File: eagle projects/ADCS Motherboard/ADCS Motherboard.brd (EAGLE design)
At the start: 91 x 91 mm, 120 parts, among them J1 HDR_10_EZFET_DEBUGGER, J3 HDR_2X5_GRPB052VWQS-RC, Q1 PMV16XN, Q2 IRLML6246TRPBF, Q3 IRLML2246TRPBF, U1 MSP430F5529IPN, U2 LMV321, U3 ADS7841E_2K5, U4 LMV321, U5 LMV321, U7 HMC1053, Y1 32.768kHz, Y2 CSTCR4M00G15L99, Y3 32.768kHz

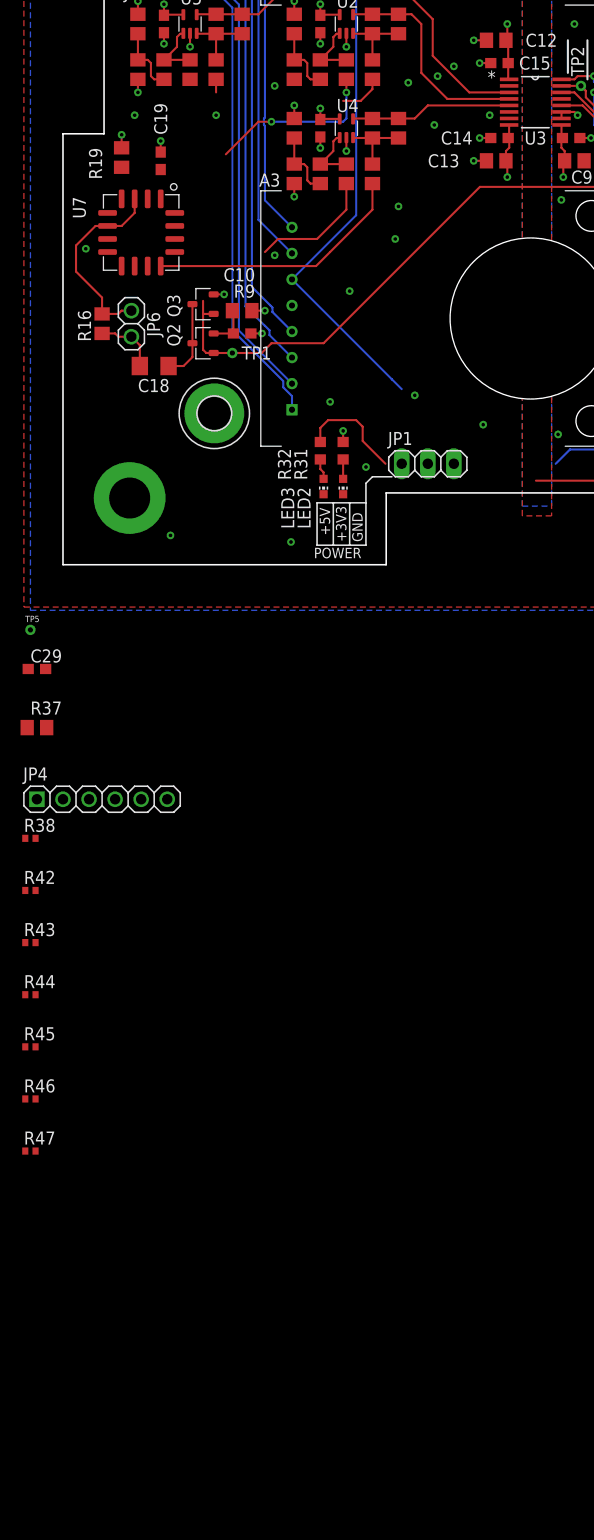
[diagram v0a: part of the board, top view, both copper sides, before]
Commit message: Added 5.1M ohms to BNO055 no connect pins
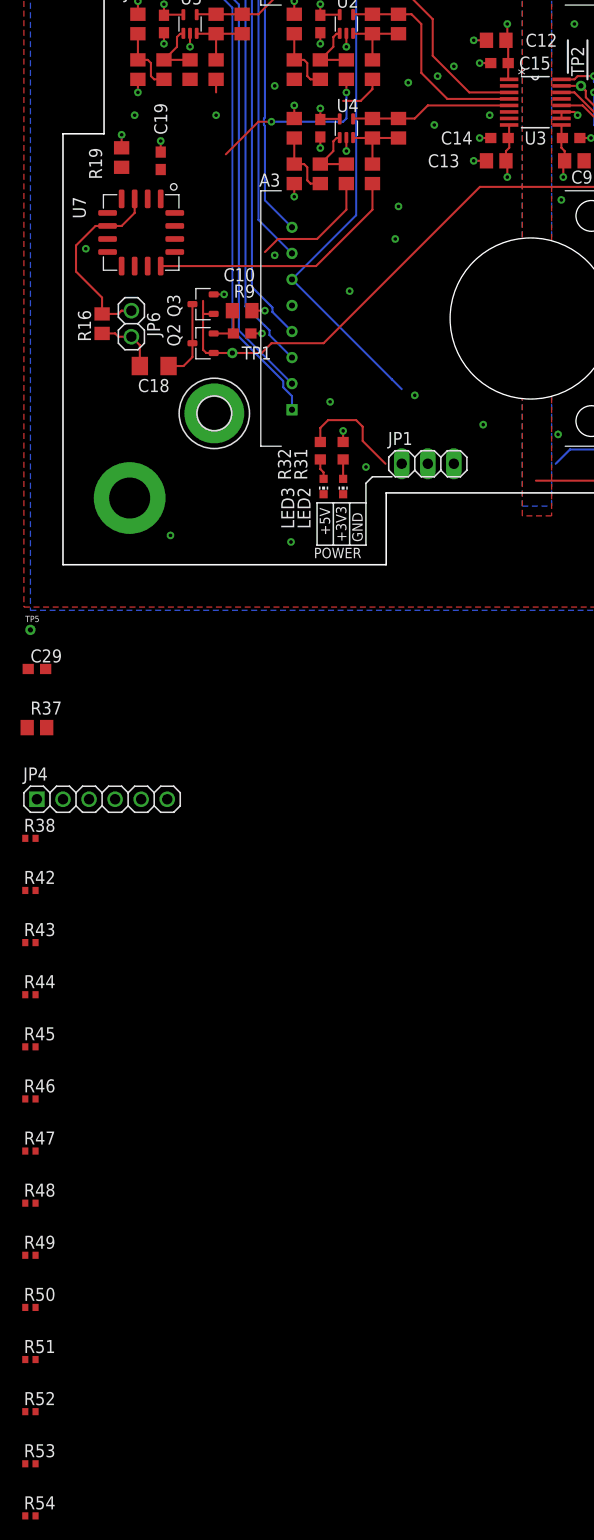
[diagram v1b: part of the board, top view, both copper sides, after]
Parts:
- added R48, R49, R50, R51, R52, R53, R54: 5.1M, rcl:R0402
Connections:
- new net N$40: R48.2, U6.1
- new net N$42: R49.2, U6.12
- new net N$43: R50.2, U6.13
- new net N$44: R51.2, U6.21
- new net N$45: R52.2, U6.22
- new net N$46: R53.2, U6.23
- new net N$47: R54.2, U6.24
- net GND: now also R48.1, R49.1, R50.1, R51.1, R52.1, R53.1, R54.1
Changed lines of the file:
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@@
 <attribute name="NAME" x="87.9475" y="13.97" size="1.27" layer="25" ratio="10" rot="R270"/>
 </element>
-<element name="U3" library="my_library" library_urn="urn:adsk.eagle:library:22876504" package="DBQ16" package3d_urn="urn:adsk.eagle:package:23087509/5" value="ADS7841E_2K5" x="46.0375" y="45.085" smashed="yes">
+<element name="U3" library="my_library" library_urn="urn:adsk.eagle:library:22876504" package="DBQ16" package3d_urn="urn:adsk.eagle:package:23087509/6" value="ADS7841E_2K5" x="46.0375" y="45.085" smashed="yes">
 <attribute name="DATASHEET_URL" value="http://www.ti.com/lit/gpn/ADS7841" x="71.4375" y="9.525" size="1.778" layer="27" display="off"/>
 <attribute name="DESCRIPTION" value="12-Bit, 4-Channel Serial Output Sampling Analog-to-Digital Converter" x="71.4375" y="9.525" size="1.778" layer="27" display="off"/>
@@
 <attribute name="SPICEPREFIX" value="R" x="-3.175" y="-57.15" size="1.778" layer="27" display="off"/>
 <attribute name="VALUE" x="-3.81" y="-59.055" size="1.27" layer="27"/>
+</element>
+<element name="R48" library="rcl" library_urn="urn:adsk.eagle:library:334" package="R0402" package3d_urn="urn:adsk.eagle:package:23547/3" value="5.1M" x="-3.175" y="-62.23" smashed="yes">
+<attribute name="NAME" x="-3.81" y="-61.595" size="1.27" layer="25"/>
+<attribute name="POPULARITY" value="34" x="-3.175" y="-62.23" size="1.778" layer="27" display="off"/>
+<attribute name="SPICEPREFIX" value="R" x="-3.175" y="-62.23" size="1.778" layer="27" display="off"/>
+<attribute name="VALUE" x="-3.81" y="-64.135" size="1.27" layer="27"/>
+</element>
+<element name="R49" library="rcl" library_urn="urn:adsk.eagle:library:334" package="R0402" package3d_urn="urn:adsk.eagle:package:23547/3" value="5.1M" x="-3.175" y="-67.31" smashed="yes">
+<attribute name="NAME" x="-3.81" y="-66.675" size="1.27" layer="25"/>
+<attribute name="POPULARITY" value="34" x="-3.175" y="-67.31" size="1.778" layer="27" display="off"/>
+<attribute name="SPICEPREFIX" value="R" x="-3.175" y="-67.31" size="1.778" layer="27" display="off"/>
+<attribute name="VALUE" x="-3.81" y="-69.215" size="1.27" layer="27"/>
+</element>
+<element name="R50" library="rcl" library_urn="urn:adsk.eagle:library:334" package="R0402" package3d_urn="urn:adsk.eagle:package:23547/3" value="5.1M" x="-3.175" y="-72.39" smashed="yes">
+<attribute name="NAME" x="-3.81" y="-71.755" size="1.27" layer="25"/>
+<attribute name="POPULARITY" value="34" x="-3.175" y="-72.39" size="1.778" layer="27" display="off"/>
+<attribute name="SPICEPREFIX" value="R" x="-3.175" y="-72.39" size="1.778" layer="27" display="off"/>
+<attribute name="VALUE" x="-3.81" y="-74.295" size="1.27" layer="27"/>
+</element>
+<element name="R51" library="rcl" library_urn="urn:adsk.eagle:library:334" package="R0402" package3d_urn="urn:adsk.eagle:package:23547/3" value="5.1M" x="-3.175" y="-77.47" smashed="yes">
+<attribute name="NAME" x="-3.81" y="-76.835" size="1.27" layer="25"/>
+<attribute name="POPULARITY" value="34" x="-3.175" y="-77.47" size="1.778" layer="27" display="off"/>
+<attribute name="SPICEPREFIX" value="R" x="-3.175" y="-77.47" size="1.778" layer="27" display="off"/>
+<attribute name="VALUE" x="-3.81" y="-79.375" size="1.27" layer="27"/>
+</element>
+<element name="R52" library="rcl" library_urn="urn:adsk.eagle:library:334" package="R0402" package3d_urn="urn:adsk.eagle:package:23547/3" value="5.1M" x="-3.175" y="-82.55" smashed="yes">
+<attribute name="NAME" x="-3.81" y="-81.915" size="1.27" layer="25"/>
+<attribute name="POPULARITY" value="34" x="-3.175" y="-82.55" size="1.778" layer="27" display="off"/>
+<attribute name="SPICEPREFIX" value="R" x="-3.175" y="-82.55" size="1.778" layer="27" display="off"/>
+<attribute name="VALUE" x="-3.81" y="-84.455" size="1.27" layer="27"/>
+</element>
+<element name="R53" library="rcl" library_urn="urn:adsk.eagle:library:334" package="R0402" package3d_urn="urn:adsk.eagle:package:23547/3" value="5.1M" x="-3.175" y="-87.63" smashed="yes">
+<attribute name="NAME" x="-3.81" y="-86.995" size="1.27" layer="25"/>
+<attribute name="POPULARITY" value="34" x="-3.175" y="-87.63" size="1.778" layer="27" display="off"/>
+<attribute name="SPICEPREFIX" value="R" x="-3.175" y="-87.63" size="1.778" layer="27" display="off"/>
+<attribute name="VALUE" x="-3.81" y="-89.535" size="1.27" layer="27"/>
+</element>
+<element name="R54" library="rcl" library_urn="urn:adsk.eagle:library:334" package="R0402" package3d_urn="urn:adsk.eagle:package:23547/3" value="5.1M" x="-3.175" y="-92.71" smashed="yes">
+<attribute name="NAME" x="-3.81" y="-92.075" size="1.27" layer="25"/>
+<attribute name="POPULARITY" value="34" x="-3.175" y="-92.71" size="1.778" layer="27" display="off"/>
+<attribute name="SPICEPREFIX" value="R" x="-3.175" y="-92.71" size="1.778" layer="27" display="off"/>
+<attribute name="VALUE" x="-3.81" y="-94.615" size="1.27" layer="27"/>
 </element>
 </elements>
@@
 <contactref element="R47" pad="2"/>
 <contactref element="U7" pad="15"/>
+<contactref element="R48" pad="1"/>
+<contactref element="R54" pad="1"/>
+<contactref element="R49" pad="1"/>
+<contactref element="R50" pad="1"/>
+<contactref element="R51" pad="1"/>
+<contactref element="R52" pad="1"/>
+<contactref element="R53" pad="1"/>
 <wire x1="73.025" y1="87.1056" x2="78.4225" y2="86.995" width="0" layer="19" extent="1-1"/>
 <wire x1="68.8975" y1="86.995" x2="73.025" y2="87.1056" width="0" layer="19" extent="1-1"/>
@@
 <wire x1="-2.675" y1="-52.07" x2="-2.675" y2="-46.99" width="0" layer="19" extent="1-1"/>
 <wire x1="-2.675" y1="-57.15" x2="-2.675" y2="-52.07" width="0" layer="19" extent="1-1"/>
+<wire x1="-3.675" y1="-62.23" x2="-2.675" y2="-57.15" width="0" layer="19" extent="1-1"/>
+<wire x1="-3.675" y1="-67.31" x2="-3.675" y2="-62.23" width="0" layer="19" extent="1-1"/>
+<wire x1="-3.675" y1="-72.39" x2="-3.675" y2="-67.31" width="0" layer="19" extent="1-1"/>
+<wire x1="-3.675" y1="-77.47" x2="-3.675" y2="-72.39" width="0" layer="19" extent="1-1"/>
+<wire x1="-3.675" y1="-82.55" x2="-3.675" y2="-77.47" width="0" layer="19" extent="1-1"/>
+<wire x1="-3.675" y1="-87.63" x2="-3.675" y2="-82.55" width="0" layer="19" extent="1-1"/>
+<wire x1="-3.675" y1="-92.71" x2="-3.675" y2="-87.63" width="0" layer="19" extent="1-1"/>
 <wire x1="10.16" y1="-22.86" x2="-3.675" y2="-26.67" width="0" layer="19" extent="1-1"/>
 </signal>
@@
 <wire x1="-3.675" y1="-57.15" x2="74.575" y2="42.2" width="0" layer="19" extent="1-1"/>
 </signal>
+<signal name="N$40">
+<contactref element="R48" pad="2"/>
+<contactref element="U6" pad="1"/>
+<wire x1="-2.675" y1="-62.23" x2="67.3375" y2="79.4" width="0" layer="19" extent="1-1"/>
+</signal>
+<signal name="N$42">
+<contactref element="R49" pad="2"/>
+<contactref element="U6" pad="12"/>
+<wire x1="-2.675" y1="-67.31" x2="64.3375" y2="82.525" width="0" layer="19" extent="1-1"/>
+</signal>
+<signal name="N$43">
+<contactref element="U6" pad="13"/>
+<contactref element="R50" pad="2"/>
+<wire x1="-2.675" y1="-72.39" x2="63.8375" y2="82.525" width="0" layer="19" extent="1-1"/>
+</signal>
+<signal name="N$44">
+<contactref element="U6" pad="21"/>
+<contactref element="R51" pad="2"/>
+<wire x1="-2.675" y1="-77.47" x2="63.3375" y2="79.4" width="0" layer="19" extent="1-1"/>
+</signal>
+<signal name="N$45">
+<contactref element="U6" pad="22"/>
+<contactref element="R52" pad="2"/>
+<wire x1="-2.675" y1="-82.55" x2="63.8375" y2="79.4" width="0" layer="19" extent="1-1"/>
+</signal>
+<signal name="N$46">
+<contactref element="U6" pad="23"/>
+<contactref element="R53" pad="2"/>
+<wire x1="-2.675" y1="-87.63" x2="64.3375" y2="79.4" width="0" layer="19" extent="1-1"/>
+</signal>
+<signal name="N$47">
+<contactref element="U6" pad="24"/>
+<contactref element="R54" pad="2"/>
+<wire x1="-2.675" y1="-92.71" x2="64.8375" y2="79.4" width="0" layer="19" extent="1-1"/>
+</signal>
 </signals>
